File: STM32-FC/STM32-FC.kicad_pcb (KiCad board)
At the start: 4 copper layers, 39 x 48.5 mm, 136 parts, among them J1 GH 1.25mm 6P, J10 GH 1.25mm 10P, J11 GH 1.25mm 6P, J12 GH 1.25mm 6P, J13 GH 1.25mm 6P, J14 GH 1.25mm 4P, J15 GH 1.25mm 4P, J16 GH 1.25mm 4P, J2 USB_C_USB2.0_14P, J3 GH 1.25mm 6P, J4 TF-06A, J5 JST ZH 1.5mm 2P, J6 PWM_Conn_3x14, J7 ZH 1.5mm 4P, J8 GH 1.25mm 4P, J9 ZH 1.5mm 3P, Q1 PMDPB30XN, Q2 PMDPB30XN, Q3 PMDPB55XP, U1 STM32F407VETx, U10 LPS22HH, U11 TMUX1104, U12 ATA6561-GBQW, U13 ATA6561-GBQW, U2 USBLC6-2SC6, U3 TPS62840, U4 STM32F103C8Tx, U5 TPS62840, U6 W25X40CLUXIG, U7 BMI323, U8 ICM-42688-P, U9 LIS2MDLTR, Y1 16MHz

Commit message: init:footprint
footprint 작업 시작
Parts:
- removed J16: GH 1.25mm 4P, JST_GH:JST_GH_SM04B-GHS-TB_04x1.25mm_Angled
- removed Q2: PMDPB30XN, Nexperia_SOT1118:Nexperia_SOT1118
- removed Q3: PMDPB55XP, Nexperia_SOT1118:Nexperia_SOT1118
- removed R38 (x2), R39 (x2), R40 (x2), R41 (x2), R42 (x2), R43 (x2), R44, R45, R46, R47: 10k, Resistor_SMD:R_0402_1005Metric
- removed R48, R49: 120, Resistor_SMD:R_0402_1005Metric
- added C18: 1uF, Capacitor_SMD:C_0402_1005Metric, F.Cu at (52.0, 88.5)
- added C38: 100nF, Capacitor_SMD:C_0402_1005Metric, F.Cu at (36.1, 88.5)
- added C39: 100nF, Capacitor_SMD:C_0402_1005Metric, F.Cu at (36.1, 90.5)
- added C40: 100nF, Capacitor_SMD:C_0402_1005Metric, F.Cu at (36.1, 92.4)
- added C41: 100nF, Capacitor_SMD:C_0402_1005Metric, F.Cu at (39.0, 88.5)
- added C42: 100nF, Capacitor_SMD:C_0402_1005Metric, F.Cu at (39.0, 90.5)
- added C43: 100nF, Capacitor_SMD:C_0402_1005Metric, F.Cu at (39.0, 92.4)
- added C44: 100nF, Capacitor_SMD:C_0402_1005Metric, F.Cu at (41.9, 88.5)
- added C45: 100nF, Capacitor_SMD:C_0402_1005Metric, F.Cu at (41.9, 90.5)
- added C46: 100nF, Capacitor_SMD:C_0402_1005Metric, F.Cu at (41.9, 92.4)
- added C47: 100nF, Capacitor_SMD:C_0402_1005Metric, F.Cu at (54.3, 80.2)
- added C48: 100nF, Capacitor_SMD:C_0402_1005Metric, F.Cu at (54.3, 82.2)
- added C49: 100nF, Capacitor_SMD:C_0402_1005Metric, F.Cu at (54.3, 70.3)
- added C50: 100nF, Capacitor_SMD:C_0402_1005Metric, F.Cu at (54.3, 72.3)
- added C51: 100nF, Capacitor_SMD:C_0402_1005Metric, F.Cu at (54.3, 74.2)
- added C52: 100nF, Capacitor_SMD:C_0402_1005Metric, F.Cu at (54.3, 76.2)
- added IC1: STM32F746NGH6, STM32F746NGH6:STM32F746NGH6, F.Cu at (0.00, -15.0)
- added L2: 2.2u, VLS201610ET-2R2M:VLS201610ET-2R2M, F.Cu at (46.9, 89.0)
- added R21: 10k, Resistor_SMD:R_0402_1005Metric, F.Cu at (57.2, 70.3)
- C1: value 10pF -> 4.7uF; moved to F.Cu
- C10, C11, C13, C15, C3, C5, D1, D6, L1, L3, R4, U3, Y1: moved to F.Cu
- C12: value 1uF -> 100nF; moved to F.Cu
- C14, C2: value 4.7uF -> 100nF; moved to F.Cu
- C16: value 4.7uF -> 1uF; moved to F.Cu
- C17, C19: value 10uF -> 100nF; moved to F.Cu
- C25: value 2.2uF -> 100nF
- C26: value 10nF -> 100nF
- C27: value 4.7uF -> 2.2uF
- C28: value 10uF -> 2.2uF
- C30, C32: value 100nF -> 4.7uF
- C31: value 220nF -> 4.7uF
- C33, C34, C35: value 100nF -> 10uF
- C36: value 100nF -> 2.2uF
- C4: value 10pF -> 100nF; moved to F.Cu
- C6, C7: value 2.2uF -> 100nF; moved to F.Cu
- C8, C9: value 100nF -> 10pF; moved to F.Cu
- J1, J3: value GH 1.25mm 6P -> SM06B-GHS-TBT; footprint JST_GH:JST_GH_SM06B-GHS-TB_06x1.25mm_Angled -> Connector_JST:JST_GH_SM06B-GHS-TB_1x06-1MP_P1.25mm_Horizontal; moved to F.Cu
- J10: value GH 1.25mm 10P -> SM06B-GHS-TBT; footprint JST_GH:JST_GH_SM10B-GHS-TB_10x1.25mm_Angled -> Connector_JST:JST_GH_SM06B-GHS-TB_1x06-1MP_P1.25mm_Horizontal
- J11: value GH 1.25mm 6P -> SM06B-GHS-TBT; footprint JST_GH:JST_GH_SM06B-GHS-TB_06x1.25mm_Angled -> Connector_JST:JST_GH_SM06B-GHS-TB_1x06-1MP_P1.25mm_Horizontal
- J12: value GH 1.25mm 6P -> PWM_Conn_3x14; footprint JST_GH:JST_GH_SM06B-GHS-TB_06x1.25mm_Angled -> PWM_Connector:PWM_Conn_3x14; moved to F.Cu
- J13: value GH 1.25mm 6P -> SM04B-GHS-TBT; footprint JST_GH:JST_GH_SM06B-GHS-TB_06x1.25mm_Angled -> Connector_JST:JST_GH_SM04B-GHS-TB_1x04-1MP_P1.25mm_Horizontal; moved to F.Cu
- J14: value GH 1.25mm 4P -> ZH 1.5mm 4P; footprint JST_GH:JST_GH_SM04B-GHS-TB_04x1.25mm_Angled -> JST_ZH:JST_ZH_S4B-ZR-SM4A-TF_1x04-1MP_P1.50mm_Horizontal; moved to F.Cu
- J15: value GH 1.25mm 4P -> SM06B-GHS-TBT; footprint JST_GH:JST_GH_SM04B-GHS-TB_04x1.25mm_Angled -> Connector_JST:JST_GH_SM06B-GHS-TB_1x06-1MP_P1.25mm_Horizontal
- J4: value TF-06A -> DM3AT-SF-PEJM5; footprint TF-06A:TF06A -> Connector_Card:microSD_HC_Hirose_DM3AT-SF-PEJM5; moved to F.Cu
- J5: value JST ZH 1.5mm 2P -> SM06B-GHS-TBT; footprint JST_ZH:JST_ZH_S2B-ZR-SM4A-TF_1x02-1MP_P1.50mm_Horizontal -> Connector_JST:JST_GH_SM06B-GHS-TB_1x06-1MP_P1.25mm_Horizontal
- J6: value PWM_Conn_3x14 -> SM06B-GHS-TBT; footprint PWM_Connector:PWM_Conn_3x14 -> Connector_JST:JST_GH_SM06B-GHS-TB_1x06-1MP_P1.25mm_Horizontal
- J7: value ZH 1.5mm 4P -> SM04B-GHS-TBT; footprint JST_ZH:JST_ZH_S4B-ZR-SM4A-TF_1x04-1MP_P1.50mm_Horizontal -> Connector_JST:JST_GH_SM04B-GHS-TB_1x04-1MP_P1.25mm_Horizontal
- J8: value GH 1.25mm 4P -> SM04B-GHS-TBT; footprint JST_GH:JST_GH_SM04B-GHS-TB_04x1.25mm_Angled -> Connector_JST:JST_GH_SM04B-GHS-TB_1x04-1MP_P1.25mm_Horizontal; moved to F.Cu
- J9: value ZH 1.5mm 3P -> SM04B-GHS-TBT; footprint JST_ZH:JST_ZH_S3B-ZR-SM4A-TF_1x03-1MP_P1.50mm_Horizontal -> Connector_JST:JST_GH_SM04B-GHS-TB_1x04-1MP_P1.25mm_Horizontal
- R1, R23, R24, R5: value 10k -> 120
- R10: value 120 -> 1k5; moved to F.Cu
- R11, R12: value 10k -> 267k; moved to F.Cu
- R13: value 5k1 -> 267k
- R14: value 5k1 -> 10k
- R15, R16, R17, R18: value 1k -> 10k; moved to F.Cu
- R19: value 1k5 -> 10k
- R2: value 10k -> 120; moved to F.Cu
- R20, R22: value 267k -> 10k; moved to F.Cu
- R29: value 15k -> 10k
- R3: value 120 -> 10k; moved to F.Cu
- R30: value 1k -> 10k
- R36: moved to B.Cu
- R7: value 120 -> 10k
- R8: value 120 -> 5k1
- R9: value 120 -> 5k1; moved to F.Cu
- U1: value STM32F407VETx -> USBLC6-2SC6; footprint Package_QFP:LQFP-100_14x14mm_P0.5mm -> Package_TO_SOT_SMD:SOT-23-6; moved to F.Cu
- U10: value LPS22HH -> W25Q32JVUUIQ; footprint Package_LGA:ST_HLGA-10_2x2mm_P0.5mm_LayoutBorder3x2y -> W25X40CLUX:USON_LUXIG_TR_HandSolder
- U11: value TMUX1104 -> ATA6561-GBQW; footprint Package_SON:USON-10_2.5x1.0mm_P0.5mm -> ATA6561:VDFN8_3X3_MCH-L
- U13: value ATA6561-GBQW -> TMUX1104; footprint ATA6561:VDFN8_3X3_MCH-L -> Package_SON:USON-10_2.5x1.0mm_P0.5mm
- U2: value USBLC6-2SC6 -> TPS62840; footprint Package_TO_SOT_SMD:SOT-23-6 -> Package_BGA:Texas_DSBGA-6_0.855x1.255mm_Layout2x3_P0.4mm_LevelC
- U4: value STM32F103C8Tx -> TPS62840; footprint Package_QFP:LQFP-48_7x7mm_P0.5mm -> Package_BGA:Texas_DSBGA-6_0.855x1.255mm_Layout2x3_P0.4mm_LevelC
- U5: value TPS62840 -> ICM-45686; footprint Package_BGA:Texas_DSBGA-6_0.855x1.255mm_Layout2x3_P0.4mm_LevelC -> ICM-45686:ICM-45686; moved to F.Cu
- U6: value W25X40CLUXIG -> ICM-45686; footprint W25X40CLUX:USON_LUXIG_TR_HandSolder -> ICM-45686:ICM-45686
- U7: value BMI323 -> BMM350; footprint BMI323:BMI323 -> BMM350:BMM350
- U8: value ICM-42688-P -> ICP-20100; footprint ICM-42688-P:IIM42352_L -> ICP-20100:ICP-20100
- U9: value LIS2MDLTR -> BMP390; footprint LIS2MDLTR:LIS2MDLTR -> BMP390:BMP390
- moved R36 193.0 mm to (-15.1, -15.2)
- moved H1 164.0 mm to (-15.0, -15.0)
- moved H2 147.6 mm to (15.0, -15.0)
- moved H4 141.4 mm to (15.0, 15.0)
- moved H3 122.1 mm to (-15.0, 15.0)
- moved J12 114.2 mm to (57.8, 137.5), turned to 180 degrees
- moved U5 101.4 mm to (132.5, 138.9), turned to 180 degrees
- moved R12 97.9 mm to (83.5, 64.3)
- moved R16 96.9 mm to (84.0, 66.3), turned to 0 degrees
- moved R17 96.9 mm to (84.0, 67.3), turned to 180 degrees
- moved R10 95.9 mm to (84.5, 64.3)
- moved R9 88.9 mm to (88.0, 64.3)
- moved R15 87.9 mm to (88.5, 67.3), turned to 180 degrees
- moved R18 87.9 mm to (88.5, 66.3), turned to 0 degrees
- moved R11 86.9 mm to (89.0, 64.3)
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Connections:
- C1 pad 1: GND -> +3.3V
- C1 pad 2: /OSC_IN -> GND
- C14 pad 1: +5V -> +3.3V
- C16 pad 1: +5V -> GND
- C16 pad 2: GND -> +3.3V
- C17 pad 1: +3.3V -> GND
- C17 pad 2: GND -> +3.3V
- C19 pad 1: +3.3V -> GND
- C19 pad 2: GND -> +3.3V
- C24 pad 1: GND -> +3.3V
- C24 pad 2: +3.3V -> GND
- C27 pad 1: GND -> Net-(IC1C-VCAP_1)
- C27 pad 2: +3.3V -> GND
- C28 pad 1: +3.3V -> GND
- C28 pad 2: GND -> Net-(IC1C-VCAP_2)
- C29 pad 1: +3.3V -> NRST
- C30 pad 1: +3.3V -> +5V
- C31 pad 1: Net-(U9-C1) -> +5V
- C32 pad 1: GND -> +5V
- C32 pad 2: +3.3V -> GND
- C33 pad 1: GND -> +3.3V
- C33 pad 2: +3.3V -> GND
- C34 pad 1: GND -> +3.3V
- C34 pad 2: +5V -> GND
- C35 pad 1: GND -> +3.3V
- C35 pad 2: +5V -> GND
- C36 pad 1: GND -> Net-(U7-CRST)
- C36 pad 2: +3.3V -> GND
- C4 pad 1: Net-(C4-Pad1) -> +3.3V
- C5 pad 1: /NRST -> +3.3V
- C6 pad 1: GND -> +3.3V
- C6 pad 2: /VCAP1 -> GND
- C7 pad 1: /VCAP2 -> +3.3V
- C8 pad 1: +3.3V -> Net-(C8-Pad1)
- C9 pad 1: +3.3V -> GND
- C9 pad 2: GND -> Net-(IC1A-PH0)
- D2 pad 2: /LED_RED -> /STM32_io/LED_RED
- D3 pad 2: /LED_YELLOW -> /STM32_io/LED_YELLOW
- D4 pad 2: /LED_GREEN -> /STM32_io/LED_GREEN
- D5 pad 2: VBUS -> +5V_PWM
- D6 pad 2: Net-(D6-A) -> VBUS
- J1 pad 4: /NRST -> NRST
- J1 pad 5: /BOOT0 -> BOOT0
- J10 pad 2: /UART4_TX -> GPS1_TX
- J10 pad 3: /UART4_RX -> GPS1_RX
- J10 pad 4: /I2C3_SCL -> GPS1_SCL
- J10 pad 5: /I2C3_SDA -> GPS1_SDA
- J10 pad 6: /GPS1_SW -> GND
- J11 pad 2: /UART5_TX -> GPS2_TX
- J11 pad 3: /UART5_RX -> GPS2_RX
- J11 pad 4: /I2C2_SCL -> GPS2_SCL
- J11 pad 5: /I2C2_SDA -> GPS2_SDA
- J12 pad 1: +5V -> MAIN1
- J12 pad 2: /UART2_TX -> MAIN2
- J12 pad 3: /UART2_RX -> MAIN3
- J12 pad 4: /UART2_CTS -> MAIN4
- J12 pad 5: /UART2_RTS -> MAIN5
- J12 pad 6: GND -> MAIN6
- J13 pad 1: +5V -> RC1_TX
- J13 pad 2: /UART3_TX -> RC1_RX
- J13 pad 3: /UART3_RX -> +5V
- J13 pad 4: /UART3_CTS -> GND
- J14 pad 1: +5V -> RC1_TX
- J14 pad 2: /I2C1_SCL -> unconnected-(J14-Pin_2-Pad2)
- J14 pad 3: /I2C1_SDA -> +5V
- J15 pad 1: +5V -> /IO/VTX_PWR
- J15 pad 2: /Communication/CAN1_P -> GND
- J15 pad 3: /Communication/CAN1_N -> VTX_TX
- J15 pad 4: GND -> VTX_RX
- J3 pad 1: Net-(D6-A) -> +5V
- J3 pad 2: Net-(D6-A) -> +5V
- J3 pad 3: /PM_CURRENT -> PM_CURRENT
- J3 pad 4: /PM_VOLTAGE -> PM_VOLTAGE
- J4 pad 1: unconnected-(J4-RSV_1-Pad1) -> SD_D2
- J4 pad 2: /MSD_NSS -> SD_D3
- J4 pad 3: /SPI2_MOSI -> SD_CMD
- J4 pad 5: /SPI2_SCK -> SD_CK
- J4 pad 7: /SPI2_MISO -> SD_D0
- J4 pad 8: unconnected-(J4-RSV_2-Pad8) -> SD_D1
- J5 pad 1: +BATT -> +5V
- J5 pad 2: GND -> TELEM1_TX
- J6 pad 1: unconnected-(J6-CH1-Pad1) -> +5V
- J6 pad 2: unconnected-(J6-CH2-Pad2) -> TELEM2_TX
- J6 pad 3: unconnected-(J6-CH3-Pad3) -> TELEM2_RX
- J6 pad 4: unconnected-(J6-CH4-Pad4) -> TELEM2_CTS
- J6 pad 5: unconnected-(J6-CH5-Pad5) -> TELEM2_RTS
- J6 pad 6: unconnected-(J6-CH6-Pad6) -> GND
- J7 pad 1: /RC_TX -> +5V
- J7 pad 2: unconnected-(J7-Pin_2-Pad2) -> I2C_SCL
- J7 pad 3: +5V -> I2C_SDA
- J8 pad 1: /RC_TX -> +5V
- J8 pad 2: /RC_RX -> /IO/CAN1_P
- J8 pad 3: +5V -> /IO/CAN1_N
- J9 pad 1: +3.3V -> +5V
- J9 pad 2: GND -> /IO/CAN2_P
- J9 pad 3: /RC_RX -> /IO/CAN2_N
- L1 pad 1: Net-(U3-SW) -> Net-(U2-SW)
- L3 pad 1: Net-(U5-SW) -> Net-(U4-SW)
- Q1 pad 3: /RC_RX -> RC1_RX
- Q1 pad 8: /RC_RX -> RC1_RX
- R1 pad 1: Net-(U1-PB2) -> Net-(C8-Pad1)
- R1 pad 2: GND -> Net-(IC1A-PH1)
- R10 pad 1: /PWR_SEL1 -> +3.3V
- R10 pad 2: Net-(Q2B-G) -> USB_D+
- R11 pad 1: Net-(Q2A-G) -> GND
- R11 pad 2: GND -> Net-(U2-VSET)
- R12 pad 1: Net-(Q2B-G) -> GND
- R12 pad 2: GND -> Net-(U3-VSET)
- R13 pad 1: Net-(J2-CC1) -> GND
- R13 pad 2: GND -> Net-(U4-VSET)
- R14 pad 1: Net-(J2-CC2) -> +3.3V
- R14 pad 2: GND -> SD_D2
- R15 pad 1: +5V -> +3.3V
- R15 pad 2: Net-(Q3A-G) -> SD_D2
- R16 pad 1: +5V -> +3.3V
- R16 pad 2: Net-(Q3B-G) -> SD_CMD
- R17 pad 1: +5V_PWM1 -> +3.3V
- R17 pad 2: GND -> SD_D0
- R18 pad 1: +5V_PWM2 -> +3.3V
- R18 pad 2: GND -> SD_D1
- R19 pad 2: /USB_D+ -> TELEM1_RX
- R2 pad 1: /BOOT0 -> /STM32_io/Buzzer
- R2 pad 2: GND -> Net-(Q1A-G)
- R20 pad 1: GND -> +3.3V
- R20 pad 2: Net-(U3-VSET) -> TELEM2_RX
- R22 pad 1: GND -> +3.3V
- R22 pad 2: Net-(U5-VSET) -> I2C_SCL
- R23 pad 1: +3.3V -> /IO/CAN1_P
- R23 pad 2: /SPI2_MISO -> /IO/CAN1_N
- R24 pad 1: +3.3V -> /IO/CAN2_P
- R24 pad 2: /SPI2_SCK -> /IO/CAN2_N
- R25 pad 2: /SPI2_MOSI -> GPS1_SDA
- R26 pad 2: /MSD_NSS -> GPS1_SCL
- R27 pad 1: /MSD_DETECT -> +3.3V
- R27 pad 2: Net-(J4-SWICTH) -> GPS2_SDA
- R28 pad 2: /BARO_NSS -> GPS1_RX
- R29 pad 1: +BATT -> +3.3V
- R29 pad 2: /V_BATT -> GPS2_SCL
- R3 pad 1: Net-(C4-Pad1) -> Net-(Q1A-G)
- R3 pad 2: /OSC_OUT -> GND
- R30 pad 1: /V_BATT -> +3.3V
- R30 pad 2: GND -> GPS2_RX
- R31 pad 1: /RC_SEL0 -> RC_SEL0
- R32 pad 1: /RC_SEL1 -> RC_SEL1
- R33 pad 1: /RC_INPUT/SBUS -> /IO/SBUS
- R35 pad 2: /RC_RX -> RC1_RX
- R36 pad 1: +3.3V -> PPM_IN
- R36 pad 2: /RC_RX -> GND
- R37 pad 1: /RC_PPM -> +3.3V
- R37 pad 2: GND -> RC1_RX
- R4 pad 1: /Buzzer -> Net-(D2-K)
- R4 pad 2: Net-(Q1A-G) -> GND
- R5 pad 1: Net-(Q1A-G) -> Net-(D3-K)
- R6 pad 1: Net-(D2-K) -> Net-(D4-K)
- R7 pad 1: Net-(D3-K) -> BOOT0
- R8 pad 1: Net-(D4-K) -> Net-(J2-CC1)
- R9 pad 1: /PWR_SEL0 -> Net-(J2-CC2)
- R9 pad 2: Net-(Q2A-G) -> GND
- U1 pad 1: /LED_GREEN -> USB_D-
- U1 pad 2: /GYRO2_NSS -> GND
- U1 pad 3: /MAG_NSS -> /USB & POWER/USB_CONN_D-
- U1 pad 4: /GYRO1_NSS -> /USB & POWER/USB_CONN_D+
- U1 pad 5: /BARO_NSS -> VBUS
- U1 pad 6: +3.3V -> USB_D+
- U10 pad 1: +3.3V -> FLASH_NSS
- U10 pad 2: /SPI1_SCK -> FLASH_MISO
- U10 pad 3: GND -> +3.3V
- U10 pad 4: /SPI1_MOSI -> GND
- U10 pad 5: /SPI1_MISO -> FLASH_MOSI
- U10 pad 6: /BARO_NSS -> FLASH_SCK
- U10 pad 7: /BARO_INT -> +3.3V
- U10 pad 8: GND -> +3.3V
- U10 pad 9: GND -> unconnected-(U10-TP-Pad9)
- U11 pad 1: /RC_SEL0 -> CAN1_TX
- U11 pad 2: /RC_PPM -> GND
- U11 pad 3: GND -> +5V
- U11 pad 4: /RC_RX -> CAN1_RX
- U11 pad 6: +3.3V -> /IO/CAN1_N
- U11 pad 7: /RC_TX -> /IO/CAN1_P
- U11 pad 8: /RC_INPUT/RCIN -> CAN1_STBY
- U11 pad 9: /RC_INPUT/SBUS -> GND
- U12 pad 1: /CAN1_TX -> CAN2_TX
- U12 pad 4: /CAN1_RX -> CAN2_RX
- U12 pad 6: /Communication/CAN1_N -> /IO/CAN2_N
- U12 pad 7: /Communication/CAN1_P -> /IO/CAN2_P
- U12 pad 8: /CAN1_STBY -> CAN2_STBY
- U13 pad 1: /CAN2_TX -> RC_SEL0
- U13 pad 2: GND -> RC1_RX
- U13 pad 3: +5V -> GND
- U13 pad 4: /CAN2_RX -> RC1_TX
- U13 pad 6: /Communication/CAN2_N -> +3.3V
- U13 pad 7: /Communication/CAN2_P -> PPM_IN
- U13 pad 8: /CAN2_STBY -> /IO/RCIN
- U13 pad 9: GND -> /IO/SBUS
- U3 pad C1: +5V -> SW_PWR_IMU
- U6 pad 1: /FLASH_NSS -> AHRS1_MISO
- U6 pad 2: /SPI2_MISO -> unconnected-(U6-RESV_2-Pad2)
- U6 pad 3: +3.3V -> unconnected-(U6-RESV_3-Pad3)
- U6 pad 4: GND -> unconnected-(U6-INT1/INT-Pad4)
- U6 pad 5: /SPI2_MOSI -> +3.3V
- U6 pad 6: /SPI2_SCK -> GND
- U6 pad 7: +3.3V -> unconnected-(U6-RESV_7-Pad7)
- U8 pad 1: /SPI1_MISO -> BARO1_NSS
- U8 pad 10: unconnected-(U8-RESV_10-Pad10) -> +3.3V
- U8 pad 2: unconnected-(U8-RESV_2-Pad2) -> AHRS1_SCK
- U8 pad 3: unconnected-(U8-RESV_3-Pad3) -> GND
- U8 pad 4: /GYRO1_INT -> AHRS1_MOSI
- U8 pad 6: GND -> AHRS1_MISO
- U8 pad 8: +3.3V -> GND
- U8 pad 9: unconnected-(U8-INT2/FSYNC/CLKIN-Pad9) -> GND
- U9 pad 1: /SPI1_SCK -> +3.3V
- U9 pad 2: unconnected-(U9-NC1-Pad2) -> AHRS1_SCK
- U9 pad 3: /MAG_NSS -> GND
- U9 pad 4: /SPI1_MOSI -> AHRS1_MOSI
- U9 pad 5: Net-(U9-C1) -> AHRS1_MISO
- U9 pad 6: GND -> BARO2_NSS
- U9 pad 7: /SPI1_MISO -> unconnected-(U9-INT-Pad7)
- U9 pad 9: +3.3V -> GND
- Y1 pad 1: /OSC_IN -> Net-(IC1A-PH0)
- Y1 pad 3: Net-(C4-Pad1) -> Net-(C8-Pad1)
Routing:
- net +3.3V: track 18.9 -> 0.00 mm, vias 2 -> 0
- net GND: track 11.2 -> 0.00 mm, vias 1 -> 0
- net /SPI3_MOSI: track 9.04 -> 0.00 mm, vias 1 -> 0
- net /SPI3_SCK: track 9.03 -> 0.00 mm, vias 1 -> 0
- net /SPI3_MISO: track 8.99 -> 0.00 mm, vias 1 -> 0
- net Net-(U9-C1): track 1.10 -> 0.00 mm

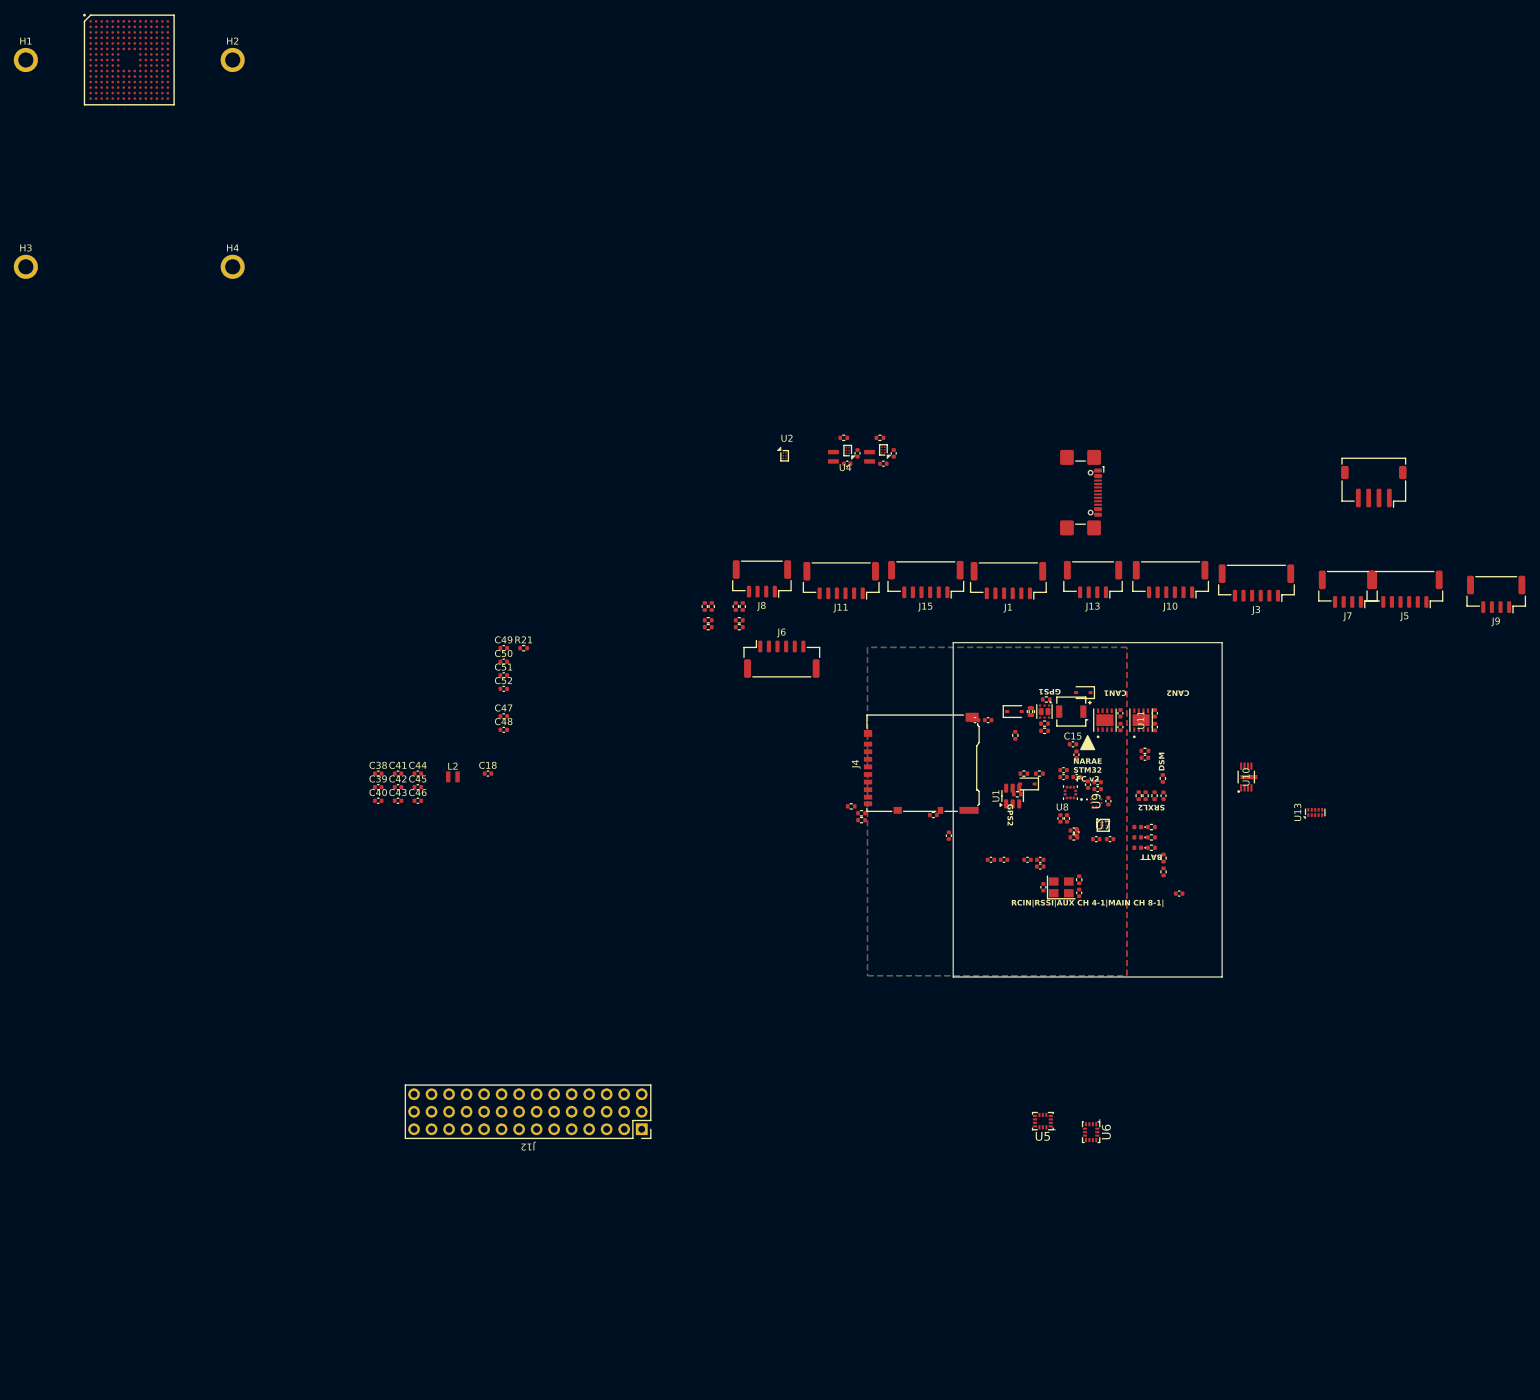
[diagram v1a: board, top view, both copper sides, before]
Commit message: change : RC size 0402 to 0201
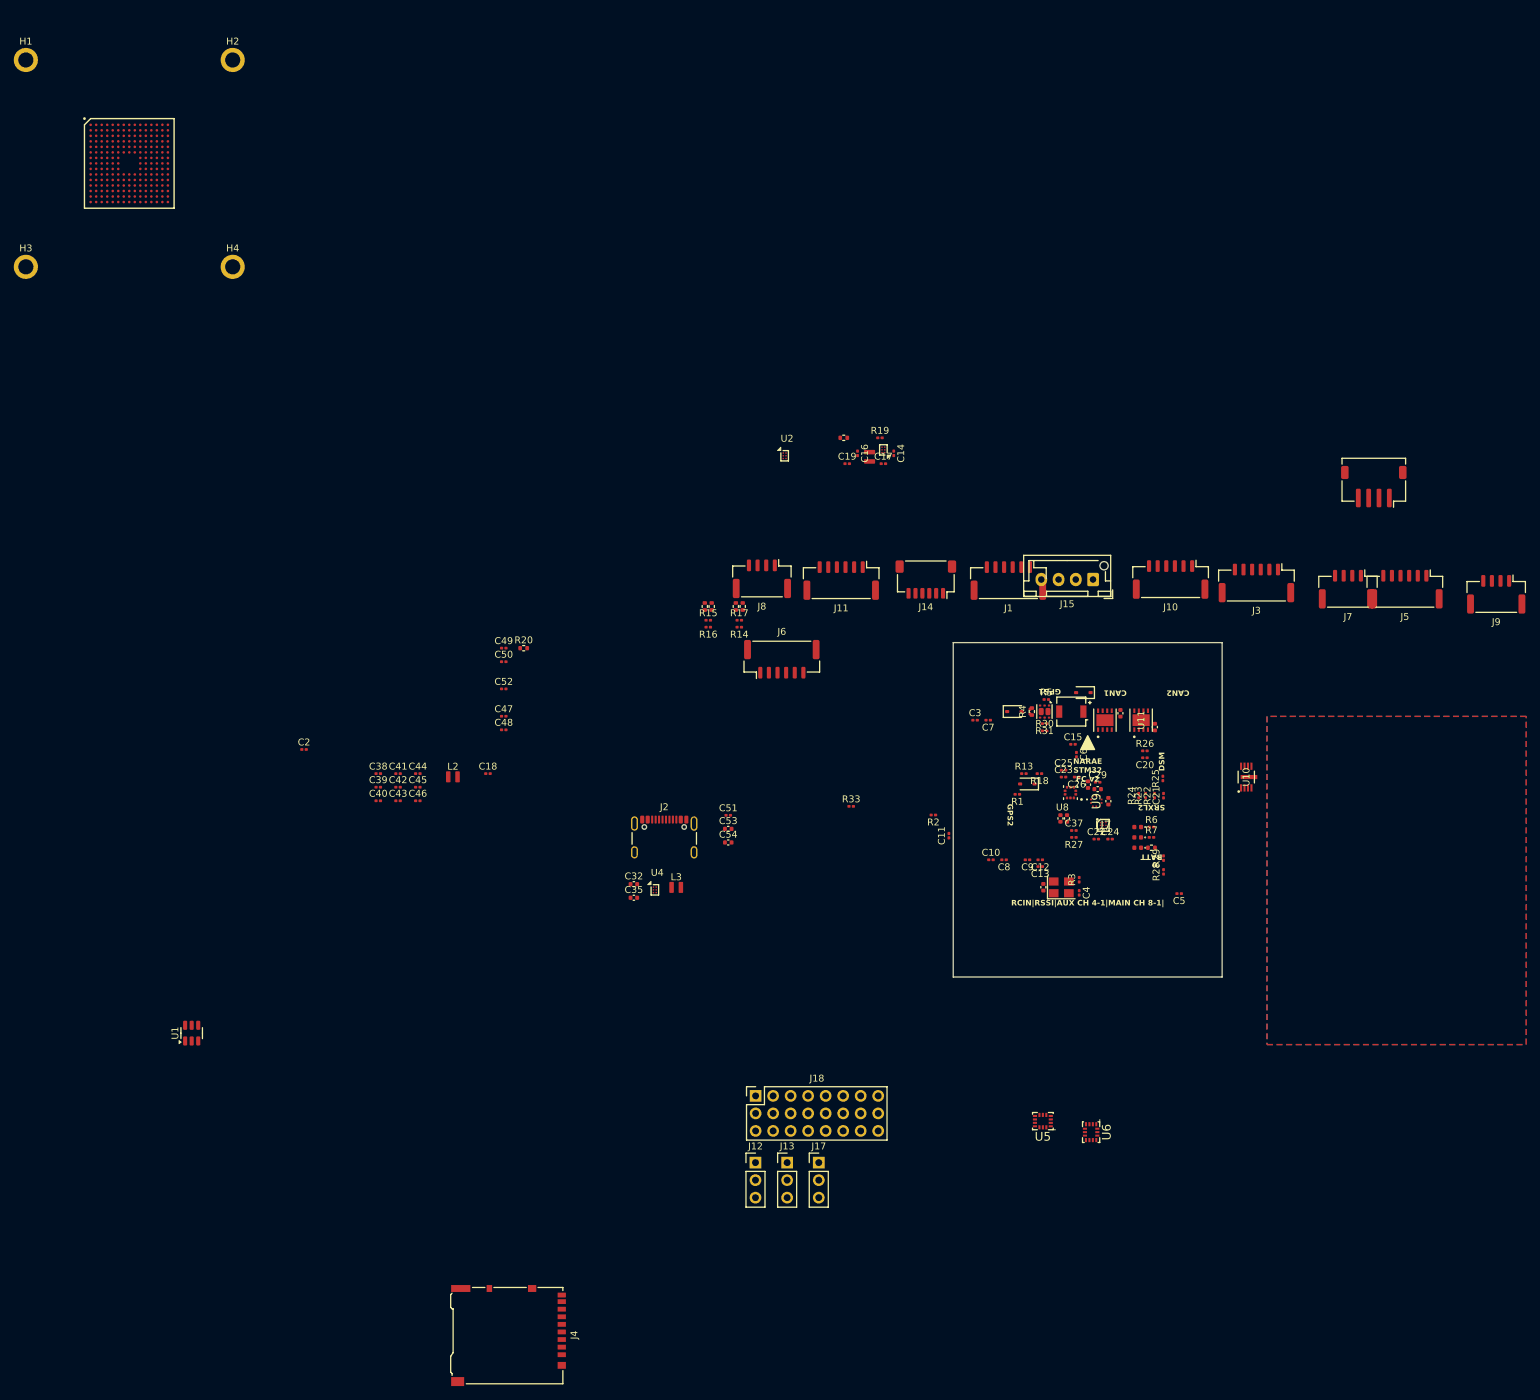
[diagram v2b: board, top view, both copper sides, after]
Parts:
- removed the R13 at (128.5, 83.0)
- removed the R31 at (106.2, 94.2)
- removed the R32 at (106.2, 95.2)
- removed R36: 10k, Resistor_SMD:R_0402_1005Metric
- removed U13: TMUX1104, Package_SON:USON-10_2.5x1.0mm_P0.5mm
- added C53: 22uF, Capacitor_SMD:C_0402_1005Metric, F.Cu at (86.9, 96.5)
- added C54: 22uF, Capacitor_SMD:C_0402_1005Metric, F.Cu at (86.9, 98.5)
- added J13: PinHeader 2.54mm, Connector_PinHeader_2.54mm:PinHeader_1x03_P2.54mm_Vertical, F.Cu at (95.4, 144.9)
- added J17: PinHeader 2.54mm, Connector_PinHeader_2.54mm:PinHeader_1x03_P2.54mm_Vertical, F.Cu at (100.0, 144.9)
- added J18: PWM_Conn_3x08, PWM_Connector:PWM_Conn_3x08, F.Cu at (99.7, 137.8)
- C10, C11, C12, C13, C14, C15, C16, C17, C18, C19, C2, C20, C21, C22, C23, C24, C25, C26, C29, C3, C37, C38, C39, C4, C40, C41, C42, C43, C44, C45, C46, C47, C48, C49, C5, C50, C51, C52, C6, C7, C8, C9: footprint Capacitor_SMD:C_0402_1005Metric -> Capacitor_SMD:C_0201_0603Metric
- J1, J10, J11, J3, J5, J6: value SM06B-GHS-TBT -> BM06B-GHS-TBT; footprint Connector_JST:JST_GH_SM06B-GHS-TB_1x06-1MP_P1.25mm_Horizontal -> Connector_JST:JST_GH_BM06B-GHS-TBT_1x06-1MP_P1.25mm_Vertical
- J12: value PWM_Conn_3x14 -> PinHeader 2.54mm; footprint PWM_Connector:PWM_Conn_3x14 -> Connector_PinHeader_2.54mm:PinHeader_1x03_P2.54mm_Vertical
- J14: renamed from J15; value SM06B-GHS-TBT -> SM06B-SRSS-TB; footprint Connector_JST:JST_GH_SM06B-GHS-TB_1x06-1MP_P1.25mm_Horizontal -> Connector_JST:JST_SH_SM06B-SRSS-TB_1x06-1MP_P1.00mm_Horizontal
- J15: renamed from J13; value SM04B-GHS-TBT -> XH_B4B; footprint Connector_JST:JST_GH_SM04B-GHS-TB_1x04-1MP_P1.25mm_Horizontal -> Connector_JST:JST_XH_B4B-XH-AM_1x04_P2.50mm_Vertical
- J2: value USB_C_USB2.0_14P -> USB_C_USB2.0_16P; footprint Connector_USB:USB_C_Receptacle_GCT_USB4110 -> Connector_USB:USB_C_Receptacle_GCT_USB4105-xx-A_16P_TopMnt_Horizontal
- J7, J8, J9: value SM04B-GHS-TBT -> BM04B-GHS-TBT; footprint Connector_JST:JST_GH_SM04B-GHS-TB_1x04-1MP_P1.25mm_Horizontal -> Connector_JST:JST_GH_BM04B-GHS-TBT_1x04-1MP_P1.25mm_Vertical
- R1, R2, R3, R4, R5, R6, R7: footprint Resistor_SMD:R_0402_1005Metric -> Resistor_SMD:R_0201_0603Metric
- R13: renamed from R14; footprint Resistor_SMD:R_0402_1005Metric -> Resistor_SMD:R_0201_0603Metric
- R14: renamed from R15; footprint Resistor_SMD:R_0402_1005Metric -> Resistor_SMD:R_0201_0603Metric
- R15: renamed from R16; footprint Resistor_SMD:R_0402_1005Metric -> Resistor_SMD:R_0201_0603Metric
- R16: renamed from R17; footprint Resistor_SMD:R_0402_1005Metric -> Resistor_SMD:R_0201_0603Metric
- R17: renamed from R18; footprint Resistor_SMD:R_0402_1005Metric -> Resistor_SMD:R_0201_0603Metric
- R18: renamed from R19; footprint Resistor_SMD:R_0402_1005Metric -> Resistor_SMD:R_0201_0603Metric
- R19: renamed from R20; footprint Resistor_SMD:R_0402_1005Metric -> Resistor_SMD:R_0201_0603Metric
- R20: renamed from R21; value 10k -> 1k5
- R21: renamed from R22; value 10k -> 1k5
- R22: renamed from R23; footprint Resistor_SMD:R_0402_1005Metric -> Resistor_SMD:R_0201_0603Metric
- R23: renamed from R24; footprint Resistor_SMD:R_0402_1005Metric -> Resistor_SMD:R_0201_0603Metric
- R24: renamed from R25; footprint Resistor_SMD:R_0402_1005Metric -> Resistor_SMD:R_0201_0603Metric
- R25: renamed from R26; footprint Resistor_SMD:R_0402_1005Metric -> Resistor_SMD:R_0201_0603Metric
- R26: renamed from R27; footprint Resistor_SMD:R_0402_1005Metric -> Resistor_SMD:R_0201_0603Metric
- R27: renamed from R28; footprint Resistor_SMD:R_0402_1005Metric -> Resistor_SMD:R_0201_0603Metric
- R28: renamed from R29; footprint Resistor_SMD:R_0402_1005Metric -> Resistor_SMD:R_0201_0603Metric
- R29: renamed from R30; footprint Resistor_SMD:R_0402_1005Metric -> Resistor_SMD:R_0201_0603Metric
- R30: renamed from R33; footprint Resistor_SMD:R_0402_1005Metric -> Resistor_SMD:R_0201_0603Metric
- R31: renamed from R34; footprint Resistor_SMD:R_0402_1005Metric -> Resistor_SMD:R_0201_0603Metric
- R33: renamed from R37; footprint Resistor_SMD:R_0402_1005Metric -> Resistor_SMD:R_0201_0603Metric
- U2, U3, U4: value TPS62840 -> TPS62840YBG
- U9: value BMP390 -> BMP390L
- moved U1 123.9 mm to (9.05, 126.1)
- moved C2 112.7 mm to (25.3, 85.0), turned to 0 degrees
- moved J4 102.3 mm to (55.0, 170.0), turned to -90 degrees
- moved C32 79.5 mm to (73.2, 104.5), turned to 0 degrees
- moved J2 78.2 mm to (77.6, 98.8), turned to 0 degrees
- moved C35 74.8 mm to (73.2, 106.5), turned to 0 degrees
- moved U4 69.6 mm to (76.2, 105.4), turned to 0 degrees
- moved L3 66.5 mm to (79.3, 105.0), turned to 0 degrees
- moved C51 38.4 mm to (86.9, 94.5)
- moved J12 33.8 mm to (90.8, 144.9), turned to 0 degrees
- moved IC1 15.0 mm to (0.00, 0.00)
- renumbered J14 to J16, R35 to R32
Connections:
- C34 pad 1: +3.3V -> +3.3VA
- C35 pad 1: +3.3V -> +1V8
- C37 pad 2: +3.3V -> +1V8
- C38 pad 1: +3.3V -> +3.3VA
- C39 pad 1: +3.3V -> +3.3VA
- C40 pad 2: +3.3V -> +3.3VA
- C41 pad 1: +3.3V -> +3.3VA
- C42 pad 1: +3.3V -> +3.3VA
- C43 pad 2: +3.3V -> +3.3VA
- C44 pad 2: +3.3V -> +3.3VA
- C45 pad 2: +3.3V -> +3.3VA
- C46 pad 2: +3.3V -> +3.3VA
- J12 pad 1: MAIN1 -> RC1_RX
- J12 pad 2: MAIN2 -> +5V
- J12 pad 3: MAIN3 -> GND
- J2 pad A8: (no net) -> unconnected-(J2-SBU1-PadA8)
- J2 pad B8: (no net) -> unconnected-(J2-SBU2-PadB8)
- L2 pad 2: +3.3V -> +3.3VA
- L3 pad 2: +3.3V -> +1V8
- U3 pad A2: +3.3V -> +3.3VA
- U4 pad A2: +3.3V -> +1V8
- U4 pad C1: SW_PWR_A -> SW_PWR_IMU
- U4 pad C2: Net-(U4-VSET) -> GND
- U5 pad 5: +3.3V -> +3.3VA
- U5 pad 8: +3.3V -> +3.3VA
- U6 pad 5: +3.3V -> +3.3VA
- U6 pad 8: +3.3V -> +3.3VA
- U7 pad B3: +3.3V -> +3.3VA
- U7 pad C1: +3.3V -> +1V8
- U8 pad 10: +3.3V -> +3.3VA
- U8 pad 5: +3.3V -> +3.3VA
- U9 pad 1: +3.3V -> +3.3VA
- U9 pad 10: +3.3V -> +3.3VA
